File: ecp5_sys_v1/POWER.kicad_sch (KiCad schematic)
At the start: 0 parts

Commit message: Finished USB schematic, left pins for future work and worked on ESP32, FPGA config, things have been confirmed, next up is thinking about power and how it will function into if the system is going to be just a DVP camera or also MIPI
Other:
- note added: "GOAL? ESP32 AND CH347F: 3V3 ECP5-85F: 1V1, 2V5, 3V3, 1V2(DDR3), 2V5(MIPI), 1V8(MIPI) DDR: 1V8, 1V2, 0V6 SEE IF YOU ACTUALLY CARE ABOUT MIPI."
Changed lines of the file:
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@@
 	(generator_version "10.0")
 	(paper "A4")
+	(text "GOAL?\n\nESP32 AND CH347F: 3V3\n	\nECP5-85F: 1V1, 2V5, 3V3, 1V2(DDR3), 2V5(MIPI), 1V8(MIPI)\n\nDDR: 1V8, 1V2, 0V6 \n\nSEE IF YOU ACTUALLY CARE ABOUT MIPI."
+		(exclude_from_sim no)
+		(at 148.844 84.074 0)
+		(effects
+			(font
+				(size 6 6)
+			)
+		)
+	)
 )

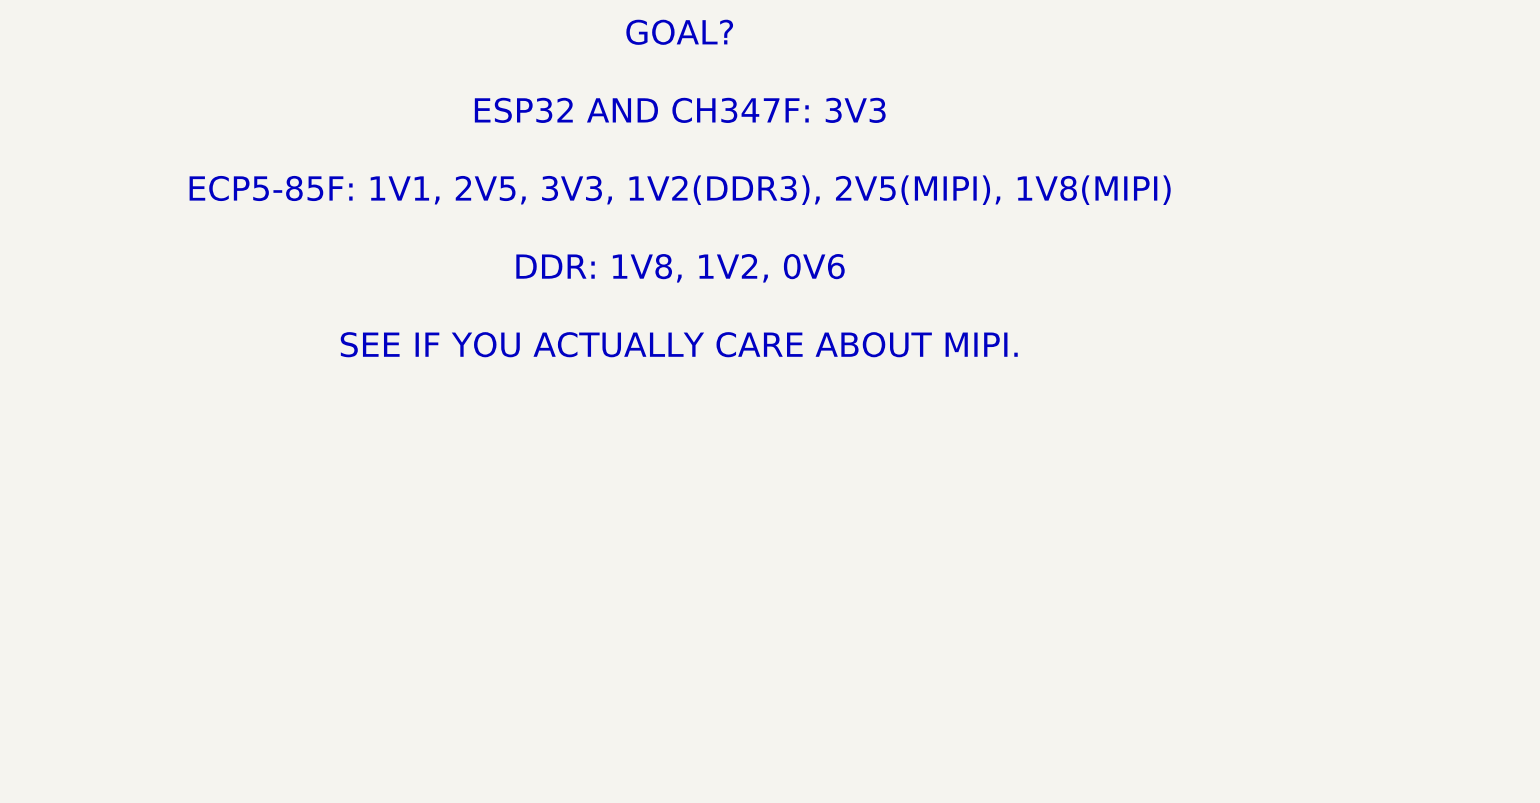
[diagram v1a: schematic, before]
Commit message: worked on power, should have external IC for sequencing and FPGA power is fine, started work in the CAMERA FPC, power 2V8 and 1V2 are there as LDOs, small package, should be fine.
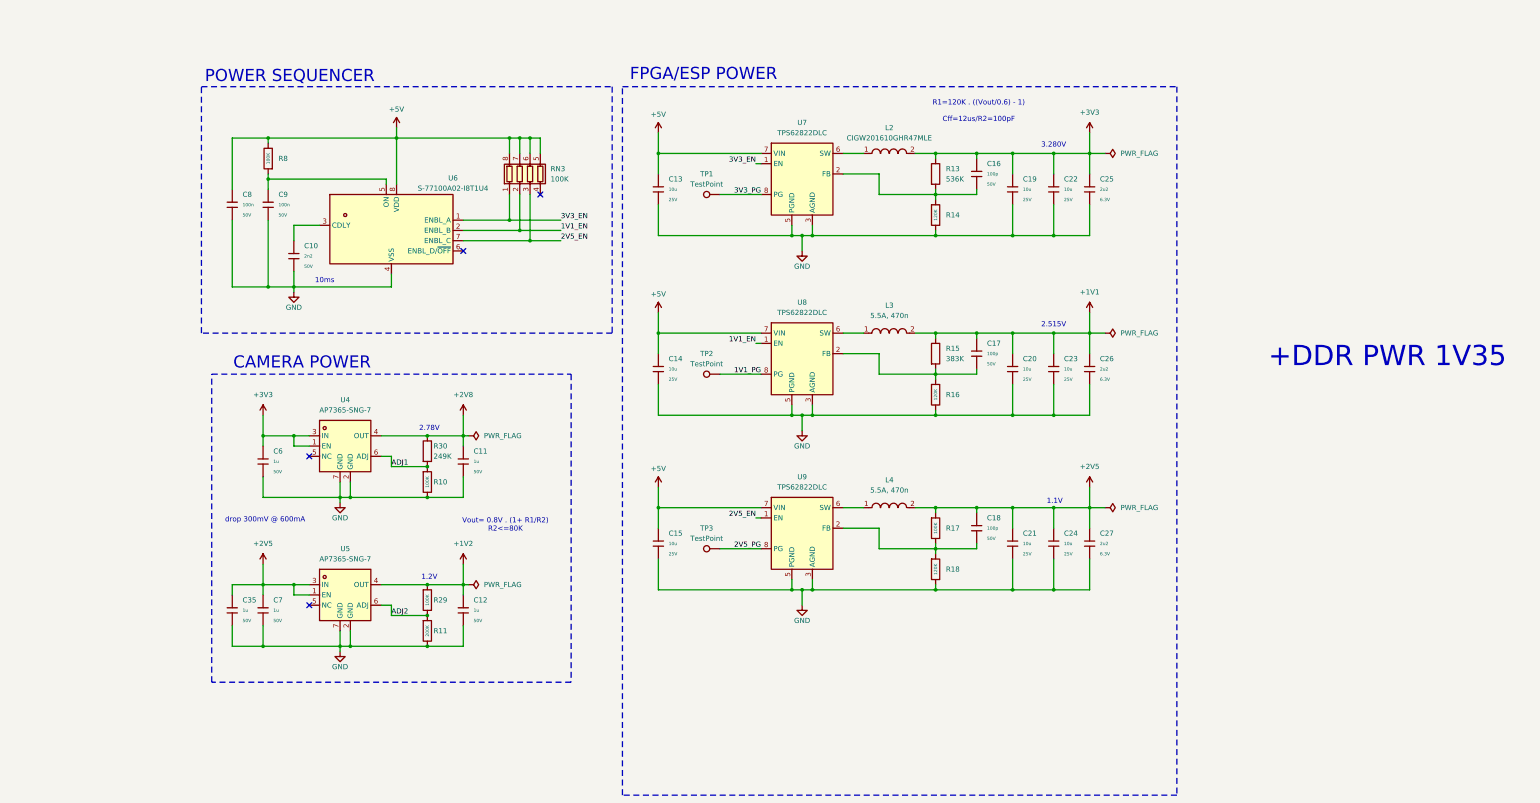
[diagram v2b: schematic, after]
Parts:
- added C10: 2n2, PCM_JLCPCB:C_0402, symbol PCM_JLCPCB-Capacitors:0402,2.2nF
- added C11, C12, C35, C6, C7: 1u, PCM_JLCPCB:C_0603, symbol PCM_JLCPCB-Capacitors:0603,1uF
- added C13, C14, C15, C19, C20, C21, C22, C23, C24: 10u, PCM_JLCPCB:C_0603, symbol PCM_JLCPCB-Capacitors:0603,10uF,(2)
- added C16, C17, C18: 100p, PCM_JLCPCB:C_0402, symbol PCM_JLCPCB-Capacitors:0402,100pF
- added C25, C26, C27: 2u2, PCM_JLCPCB:C_0402, symbol PCM_JLCPCB-Capacitors:0402,2.2uF
- added C8, C9: 100n, PCM_JLCPCB:C_0402, symbol PCM_JLCPCB-Capacitors:0402,100nF,(2)
- added L2: CIGW201610GHR47MLE, EasyEDA:L0806, symbol EasyEDA:CIGW201610GHR47MLE
- added L3, L4: 5.5A, 470n, EasyEDA:L0806, symbol EasyEDA:CIGW201610GHR47MLE
- added R10, R17, R29, R8: 100K, PCM_JLCPCB:R_0402, symbol PCM_JLCPCB-Resistors:0402,100kΩ
- added R11: 200K, PCM_JLCPCB:R_0402, symbol PCM_JLCPCB-Resistors:0402,200kΩ
- added R13: 536K, PCM_JLCPCB:R_0402, symbol Device:R
- added R14, R16, R18: 120K, PCM_JLCPCB:R_0402, symbol PCM_JLCPCB-Resistors:0402,120kΩ
- added R15: 383K, PCM_JLCPCB:R_0402, symbol Device:R
- added R30: 249K, PCM_JLCPCB:R_0402, symbol Device:R
- added RN3: 100K, PCM_Resistor_SMD_AKL:R_Array_Concave_4x0402, symbol PCM_Resistor_AKL:R_4x0402_Concave
- added TP1, TP2, TP3: TestPoint, symbol Connector:TestPoint
- added U4, U5: AP7365-SNG-7, EasyEDA:U-DFN2020-6_L2.0-W2.0-P0.65-BL-EP, symbol EasyEDA:AP7365-SNG-7
- added U6: S-77100A02-I8T1U4, EasyEDA:SNT-8A_L2.0-W2.2-P0.50-LS2.5-TL, symbol EasyEDA:S-77100A02-I8T1U4
- added U7, U8, U9: TPS62822DLC, Package_SON:Texas_VSON-HR-8_1.5x2mm_P0.5mm, symbol Regulator_Switching:TPS62822DLC
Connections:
- new net: C10.1, U6.3 (CDLY)
- new net: C17.2, R15.2, R16.1, U8.2 (FB)
- new net: L3.1, U8.6 (SW)
- new net: L4.1, U9.6 (SW)
- new net: C9.1, R8.1, U6.5 (ON)
- new net: C16.2, R13.2, R14.1, U7.2 (FB)
- new net: L2.1, U7.6 (SW)
- new net: C18.2, R17.2, R18.1, U9.2 (FB)
- new net +1V1: C17.1, C20.1, C23.1, C26.1, L3.2, R15.1
- new net +1V2: C12.1, R29.1, U5.4 (OUT)
- new net +2V5: C18.1, C21.1, C24.1, C27.1, C35.1, C7.1, L4.2, R17.1, U5.1 (EN), U5.3 (IN)
- new net +2V8: C11.1, R30.1, U4.4 (OUT)
- new net +3V3: C16.1, C19.1, C22.1, C25.1, C6.1, L2.2, R13.1, U4.1 (EN), U4.3 (IN)
- new net +5V: C13.1, C14.1, C15.1, C8.1, R8.2, RN3.5 (R4.2), RN3.6 (R3.2), RN3.7 (R2.2), RN3.8 (R1.2), U6.8 (VDD), U7.7 (VIN), U8.7 (VIN), U9.7 (VIN)
- new net 1V1_EN: RN3.2 (R2.1), U6.2 (ENBL_B), U8.1 (EN)
- new net 1V1_PG: TP2.1, U8.8 (PG)
- new net 2V5_EN: RN3.3 (R3.1), U6.7 (ENBL_C), U9.1 (EN)
- new net 2V5_PG: TP3.1, U9.8 (PG)
- new net 3V3_EN: RN3.1 (R1.1), U6.1 (ENBL_A), U7.1 (EN)
- new net 3V3_PG: TP1.1, U7.8 (PG)
- new net ADJ1: R10.1, R30.2, U4.6 (ADJ)
- new net ADJ2: R11.1, R29.2, U5.6 (ADJ)
- new net GND: C10.2, C11.2, C12.2, C13.2, C14.2, C15.2, C19.2, C20.2, C21.2, C22.2, C23.2, C24.2, C25.2, C26.2, C27.2, C35.2, C6.2, C7.2, C8.2, C9.2, R10.2, R11.2, R14.2, R16.2, R18.2, U4.2 (GND), U4.7 (GND), U5.2 (GND), U5.7 (GND), U6.4 (VSS), U7.3 (AGND), U7.5 (PGND), U8.3 (AGND), U8.5 (PGND), U9.3 (AGND), U9.5 (PGND)
- no-connect marks 0 -> 4
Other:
- note added: "+DDR PWR 1V35"
- note added: "1.1V"
- note added: "1.2V"
- note added: "10ms"
- note added: "2.515V"
- note added: "2.78V"
- note added: "3.280V"
- note added: "CAMERA POWER"
- note added: "FPGA/ESP POWER"
- note added: "POWER SEQUENCER"
- note added: "R1=120K . ((Vout/0.6) - 1) Cff=12us/R2=100pF"
- note added: "Vout= 0.8V . (1+ R1/R2) R2<=80K"
- note added: "drop 300mV @ 600mA"
- note removed: "GOAL? ESP32 AND CH347F: 3V3 ECP5-85F: 1V1, 2V5, 3V3, 1V2(DDR3), 2V5(MIPI), 1V8(MIPI) DDR: 1V8, 1V2, 0V6 SEE IF YOU ACTUALLY CARE ABOUT MIPI."
